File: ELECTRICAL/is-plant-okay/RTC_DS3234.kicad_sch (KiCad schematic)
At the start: 1 part

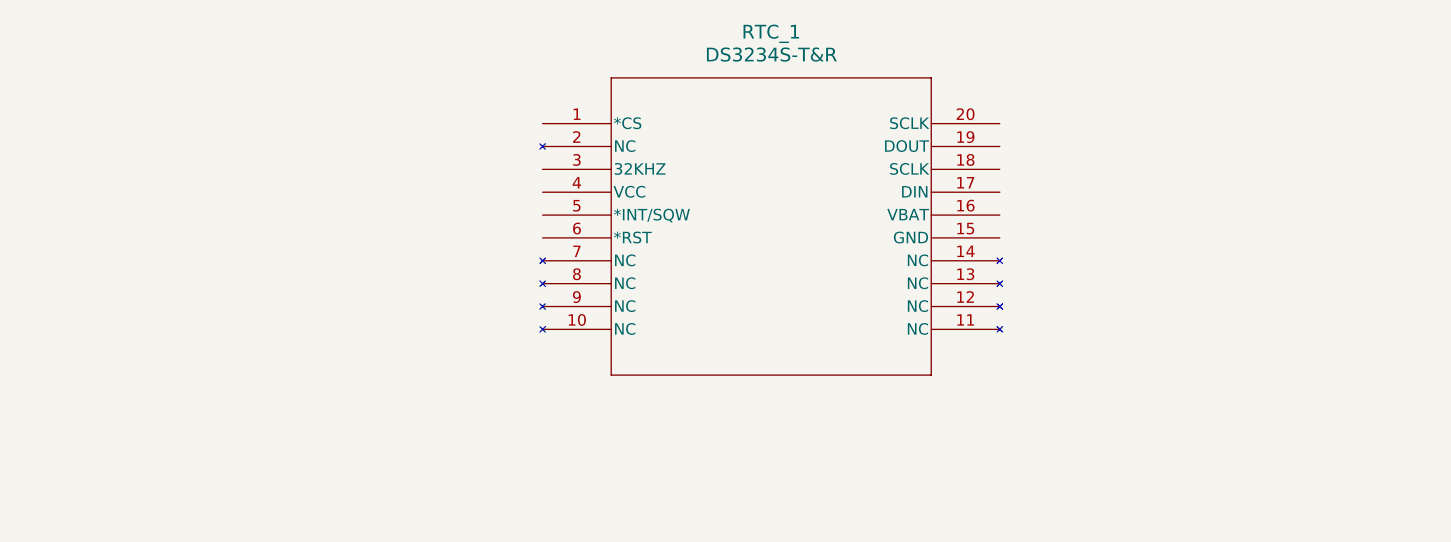
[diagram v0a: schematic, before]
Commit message: feat: add coin cell footprint
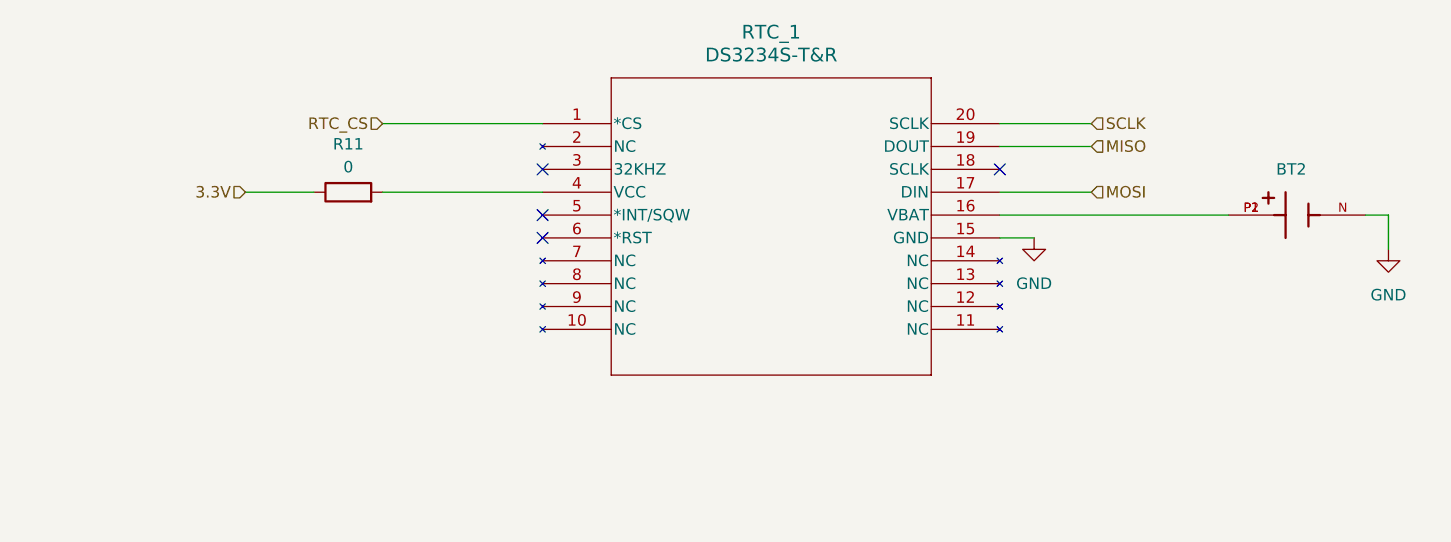
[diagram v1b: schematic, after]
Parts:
- added BT2: BAT-HLD-003-SMT, is-plant-okay-foot:BAT_BAT-HLD-003-SMT, symbol is-plant-okay-lib:BAT-HLD-003-SMT
- added R11: 0, symbol Device:R
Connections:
- net RTC_CS: now reaches RTC_1.1 (*CS)
- net GND: now reaches RTC_1.15 (GND)
- net GND: now also BT2.N
- net at RTC_1.16 (VBAT): now also BT2.P1, BT2.P2
- net MOSI: now reaches RTC_1.17 (DIN)
- net MISO: now reaches RTC_1.19 (DOUT)
- net SCLK: now reaches RTC_1.20 (SCLK)
- net at RTC_1.4 (VCC): now also R11.2
- new net 3.3V: R11.1
- no-connect marks 0 -> 4

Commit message: feat: add usb and esd protection device
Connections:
- net RTC_RST: now reaches RTC_1.6 (*RST)
- no-connect marks 4 -> 3
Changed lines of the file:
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@@
-	)
-	(no_connect
-		(at 124.46 87.63)
 	)
 	(no_connect
@@
 	(wire
 		(pts
+			(xy 106.68 87.63) (xy 124.46 87.63)
+		)
+		(stroke
+			(width 0)
+			(type default)
+		)
+	)
+	(wire
+		(pts
 			(xy 175.26 85.09) (xy 200.66 85.09)
 		)
@@
 		)
 	)
+	(hierarchical_label "RTC_RST"
+		(shape input)
+		(at 106.68 87.63 180)
+		(effects
+			(font
+				(size 1.27 1.27)
+			)
+			(justify right)
+		)
+	)

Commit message: feat: add pins for mcu
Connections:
- net MISO renamed RTC_MISO
- net MOSI renamed RTC_MOSI
- net SCLK renamed RTC_SCLK
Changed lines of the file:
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@@
 		)
 	)
-	(hierarchical_label "MISO"
+	(hierarchical_label "RTC_MISO"
 		(shape input)
 		(at 185.42 77.47 0)
@@
 		)
 	)
-	(hierarchical_label "MOSI"
+	(hierarchical_label "RTC_MOSI"
 		(shape input)
 		(at 185.42 82.55 0)
@@
 		)
 	)
-	(hierarchical_label "SCLK"
+	(hierarchical_label "RTC_SCLK"
 		(shape input)
 		(at 185.42 74.93 0)

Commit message: feat: add pins for bootloader programmer
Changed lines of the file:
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@@
 	)
 	(hierarchical_label "RTC_RST"
-		(shape input)
+		(shape output)
 		(at 106.68 87.63 180)
 		(effects
@@
 	)
 	(hierarchical_label "RTC_MISO"
-		(shape input)
+		(shape output)
 		(at 185.42 77.47 0)
 		(effects

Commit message: feat: finished schematics
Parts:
- removed R11: 0, symbol Device:R
- added SW2: RTC_RST, symbol Switch:SW_Push
- added TP5: RTC_3.3V_TP, TestPoint:TestPoint_Keystone_5000-5004_Miniature, symbol Connector:TestPoint
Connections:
- net 3.3V: now also RTC_1.4 (VCC), TP5.1
- net GND: now also SW2.1
- net at BT2.P1, RTC_1.16 (VBAT): no longer BT2.P2
- net RTC_RST: no longer names the net of RTC_1.6 (*RST)
- net RTC_RST: now also SW2.2

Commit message: feat: add resistor footprint
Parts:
- removed SW2: RTC_RST, symbol Switch:SW_Push
- added S2: RTC_RST, is-plant-okay-foot:SW_TS04-66-55-BK-260-SMT, symbol is-plant-okay-lib:TS04-66-55-BK-260-SMT
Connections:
- net GND: now also S2.2, S2.4
- net at RTC_1.6 (*RST): now also S2.3
- no-connect marks 3 -> 4
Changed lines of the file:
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@@
+		(color 0 0 0 0)
+	)
+	(junction
+		(at 86.36 113.03)
+		(diameter 0)
 		(color 0 0 0 0)
 	)
@@
 	)
 	(no_connect
+		(at 72.39 97.79)
+	)
+	(no_connect
 		(at 124.46 80.01)
 	)
@@
 	(wire
 		(pts
-			(xy 68.58 87.63) (xy 68.58 92.71)
+			(xy 97.79 107.95) (xy 100.33 107.95)
+		)
+		(stroke
+			(width 0)
+			(type default)
+		)
+	)
+	(wire
+		(pts
+			(xy 100.33 87.63) (xy 124.46 87.63)
 		)
 		(stroke
@@
 	(wire
 		(pts
+			(xy 69.85 107.95) (xy 72.39 107.95)
+		)
+		(stroke
+			(width 0)
+			(type default)
+		)
+	)
+	(wire
+		(pts
 			(xy 175.26 74.93) (xy 185.42 74.93)
 		)
@@
 	(wire
 		(pts
+			(xy 100.33 107.95) (xy 100.33 113.03)
+		)
+		(stroke
+			(width 0)
+			(type default)
+		)
+	)
+	(wire
+		(pts
 			(xy 175.26 87.63) (xy 179.07 87.63)
 		)
@@
 	(wire
 		(pts
-			(xy 73.66 87.63) (xy 68.58 87.63)
-		)
-		(stroke
-			(width 0)
-			(type default)
-		)
-	)
-	(wire
-		(pts
-			(xy 83.82 87.63) (xy 124.46 87.63)
-		)
-		(stroke
-			(width 0)
-			(type default)
-		)
-	)
-	(wire
-		(pts
 			(xy 204.47 85.09) (xy 205.74 85.09)
 		)
@@
 	(wire
 		(pts
+			(xy 86.36 113.03) (xy 69.85 113.03)
+		)
+		(stroke
+			(width 0)
+			(type default)
+		)
+	)
+	(wire
+		(pts
+			(xy 69.85 113.03) (xy 69.85 107.95)
+		)
+		(stroke
+			(width 0)
+			(type default)
+		)
+	)
+	(wire
+		(pts
 			(xy 97.79 82.55) (xy 102.87 82.55)
+		)
+		(stroke
+			(width 0)
+			(type default)
+		)
+	)
+	(wire
+		(pts
+			(xy 97.79 97.79) (xy 100.33 97.79)
+		)
+		(stroke
+			(width 0)
+			(type default)
+		)
+	)
+	(wire
+		(pts
+			(xy 100.33 113.03) (xy 86.36 113.03)
+		)
+		(stroke
+			(width 0)
+			(type default)
+		)
+	)
+	(wire
+		(pts
+			(xy 100.33 97.79) (xy 100.33 87.63)
 		)
 		(stroke
@@
 	(symbol
 		(lib_id "power:GND")
-		(at 68.58 92.71 0)
+		(at 86.36 113.03 0)
 		(unit 1)
 		(exclude_from_sim no)
@@
 		(fields_autoplaced yes)
 		(property "Reference" "#PWR06"
-			(at 68.58 99.06 0)
+			(at 86.36 119.38 0)
 			(effects
 				(font
@@
 		)
 		(property "Value" "GND"
-			(at 68.58 97.79 0)
+			(at 86.36 118.11 0)
 			(effects
 				(font
@@
 		)
 		(property "Footprint" ""
-			(at 68.58 92.71 0)
+			(at 86.36 113.03 0)
 			(effects
 				(font
@@
 		)
 		(property "Datasheet" ""
-			(at 68.58 92.71 0)
+			(at 86.36 113.03 0)
 			(effects
 				(font
@@
 		)
 		(property "Description" "Power symbol creates a global label with name \"GND\" , ground"
-			(at 68.58 92.71 0)
+			(at 86.36 113.03 0)
 			(effects
 				(font
@@
 		)
 		(instances
-			(project "is-plant-okay"
+			(project ""
 				(path "/ac51c2f9-77a4-4b89-b63f-6e0ba02b1e45/09e2268a-4f06-4551-b501-1a158603660c"
 					(reference "#PWR06")
+					(unit 1)
+				)
+			)
+		)
+	)
+	(symbol
+		(lib_id "is-plant-okay-lib:TS04-66-55-BK-260-SMT")
+		(at 85.09 102.87 0)
+		(unit 1)
+		(exclude_from_sim no)
+		(in_bom yes)
+		(on_board yes)
+		(dnp no)
+		(fields_autoplaced yes)
+		(property "Reference" "S2"
+			(at 85.09 90.17 0)
+			(effects
+				(font
+					(size 1.27 1.27)
+				)
+			)
+		)
+		(property "Value" "RTC_RST"
+			(at 85.09 92.71 0)
+			(effects
+				(font
+					(size 1.27 1.27)
+				)
+			)
+		)
+		(property "Footprint" "is-plant-okay-foot:SW_TS04-66-55-BK-260-SMT"
+			(at 85.09 102.87 0)
+			(effects
+				(font
+					(size 1.27 1.27)
+				)
+				(justify bottom)
+				(hide yes)
+			)
+		)
+		(property "Datasheet" "https://www.sameskydevices.com/product/resource/ts04.pdf"
+			(at 85.09 102.87 0)
+			(effects
+				(font
+					(size 1.27 1.27)
+				)
+				(hide yes)
+			)
+		)
+		(property "Description" "SWITCH TACTILE SPST-NO 0.05A 12V"
+			(at 85.09 102.87 0)
+			(effects
+				(font
+					(size 1.27 1.27)
+				)
+				(hide yes)
+			)
+		)
+		(property "MANUFACTURER" "CUI Devices"
+			(at 85.09 102.87 0)
+			(effects
+				(font
+					(size 1.27 1.27)
+				)
+				(justify bottom)
+				(hide yes)
+			)
+		)
+		(property "MFG PART #" "TS04-66-55-BK-260-SMT"
+			(at 85.09 102.87 0)
+			(effects
+				(font
+					(size 1.27 1.27)
+				)
+				(hide yes)
+			)
+		)
+		(property "TYPE" "SMD"
+			(at 85.09 102.87 0)
+			(effects
+				(font
+					(size 1.27 1.27)
+				)
+				(hide yes)
+			)
+		)
+		(property "PACKAGE" "~"
+			(at 85.09 102.87 0)
+			(effects
+				(font
+					(size 1.27 1.27)
+				)
+				(hide yes)
+			)
+		)
+		(pin "4"
+		)
+		(pin "2"
+		)
+		(pin "1"
+		)
+		(pin "3"
+		)
+		(instances
+			(project ""
+				(path "/ac51c2f9-77a4-4b89-b63f-6e0ba02b1e45/09e2268a-4f06-4551-b501-1a158603660c"
+					(reference "S2")
 					(unit 1)
 				)
@@
 					(unit 1)
 				)
-			)
-		)
-	)
-	(symbol
-		(lib_id "Switch:SW_Push")
-		(at 78.74 87.63 0)
-		(unit 1)
-		(exclude_from_sim no)
-		(in_bom yes)
-		(on_board yes)
-		(dnp no)
-		(fields_autoplaced yes)
-		(property "Reference" "SW2"
-			(at 78.74 80.01 0)
-			(effects
-				(font
-					(size 1.27 1.27)
-				)
-			)
-		)
-		(property "Value" "RTC_RST"
-			(at 78.74 82.55 0)
-			(effects
-				(font
-					(size 1.27 1.27)
-				)
-			)
-		)
-		(property "Footprint" ""
-			(at 78.74 82.55 0)
-			(effects
-				(font
-					(size 1.27 1.27)
-				)
-				(hide yes)
-			)
-		)
-		(property "Datasheet" "~"
-			(at 78.74 82.55 0)
-			(effects
-				(font
-					(size 1.27 1.27)
-				)
-				(hide yes)
-			)
-		)
-		(property "Description" "Push button switch, generic, two pins"
-			(at 78.74 87.63 0)
-			(effects
-				(font
-					(size 1.27 1.27)
-				)
-				(hide yes)
-			)
-		)
-		(pin "2"
-		)
-		(pin "1"
-		)
-		(instances
-			(project ""
-				(path "/ac51c2f9-77a4-4b89-b63f-6e0ba02b1e45/09e2268a-4f06-4551-b501-1a158603660c"
-					(reference "SW2")
-					(unit 1)
-				)
